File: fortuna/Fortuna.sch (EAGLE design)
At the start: 36 parts, among them M1 MOTOR20MM, M2 MOTOR20MM, Q1 600mA/40V, Q2 600mA/40V, U2 OPA2343UA, U3 OPA2343UA

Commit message: Finish fortuna schematic
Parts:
- removed C1, C2: 10uF, SparkFun-Capacitors:10UF-POLAR-RADIAL-2.5MM-25V-20%
- removed U1: (no value), SparkFun-IC-Power:V_REG_78XX-TO-220
- C3: value 1uF -> 1μF
- D3: value (none) -> LLED
- D4: value (none) -> RLED
- R1, R10, R2, R3, R4, R5, R6: value 2.7k -> 2.7kΩ
- R11: value 100k -> 100kΩ
- R12, R13, R9: value 10k -> 10kΩ
- R14, R15: value 1k -> 1kΩ
- R16, R17: value 300 -> 300Ω
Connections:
- net N$11 renamed -RPHOTO
- net N$12 renamed D2
- net N$14 renamed -MIC
- net N$15 renamed A3
- net N$25 renamed D5
- net N$26 renamed D10
- net N$4 renamed +MIC
- net N$6 renamed +RPHOTO
- net N$7 renamed -LPHOTO
- net N$9 renamed +LPHOTO
- removed net N$1 (its old number): B1.VIN, C1.+, D1.C, D2.C, G1.+, M1.+, M2.+, R9.2, U1.IN
- removed net N$10 (its old number): B1.A0, R1.1, R7.P$2
- removed net N$16: B1.D4, D3.A, U2.OUT_A
- removed net N$19: B1.D7, D4.A, U3.OUT_A
- removed net N$2 (its old number): B1.GND@0, C1.-, C2.-, G1.-, LS1.1, MK1.2, Q1.E, Q2.E, R12.1, R16.1, R17.1, R2.1, R3.2, R5.1, R6.1, U1.GND, U2.V-, U3.V-
- removed net N$22: B1.A5, R4.2, R8.P$2
- removed net N$3: C2.+, R13.1, U1.OUT, U2.V+, U3.V+
- removed net N$5: LS1.2, U3.-IN_B, U3.OUT_B
- new net 5V: B1.5V, R1.1, R13.1, R4.2, R7.P$2, R8.P$2, U2.V+, U3.V+
- new net A0: B1.A0, D3.A, U2.OUT_A
- new net A5: B1.A5, D4.A, U3.OUT_A
- new net GND: B1.GND@2, G1.-, LS1.2, MK1.2, Q1.E, Q2.E, R12.1, R16.1, R17.1, R2.1, R3.2, R5.1, R6.1, U2.V-, U3.V-
- new net OUT_BUZZER: LS1.1, U3.-IN_B, U3.OUT_B
- new net VIN: B1.VIN, D1.C, D2.C, G1.+, M1.+, M2.+, R9.2
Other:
- note added: "+BUZZER"
- note added: "-BUZZER"
- note added: "OUT_LPHOTO"
- note added: "OUT_MIC"
- note added: "OUT_RPHOTO"
- moved on the sheet: B1, C3, D1, D2, D3, D4, G1, LS1, M1, M2, MK1, Q1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

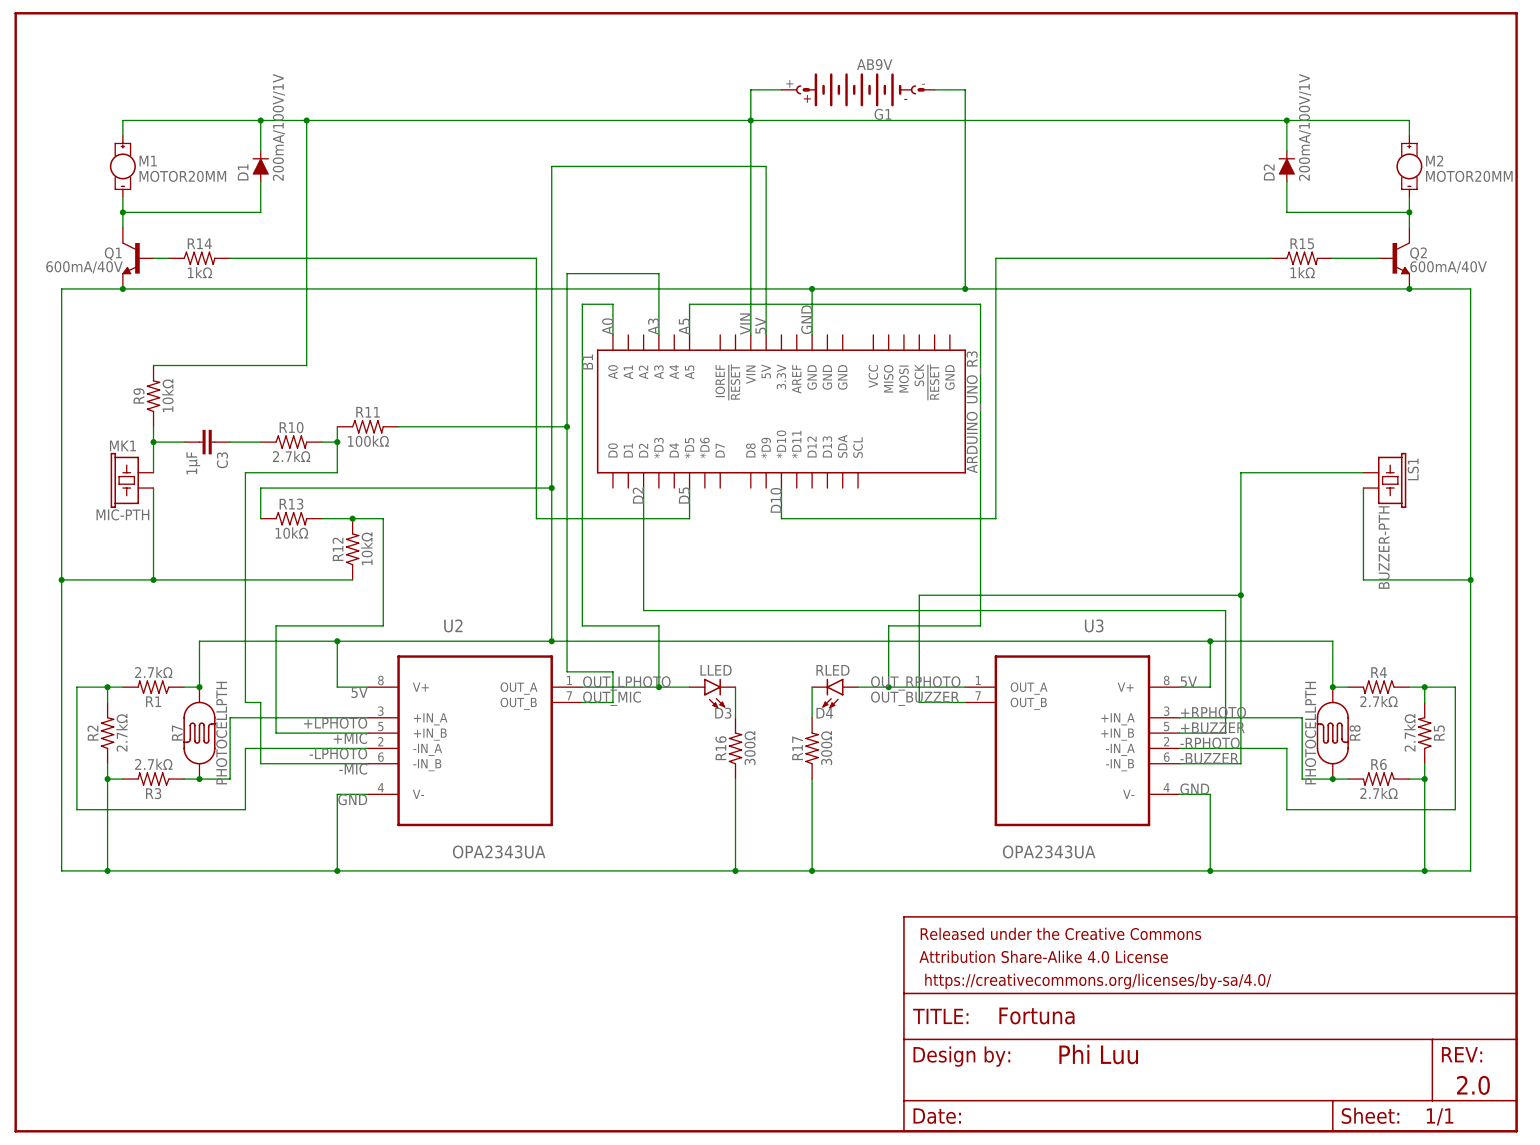
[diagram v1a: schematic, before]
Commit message: Change battery Fortuna
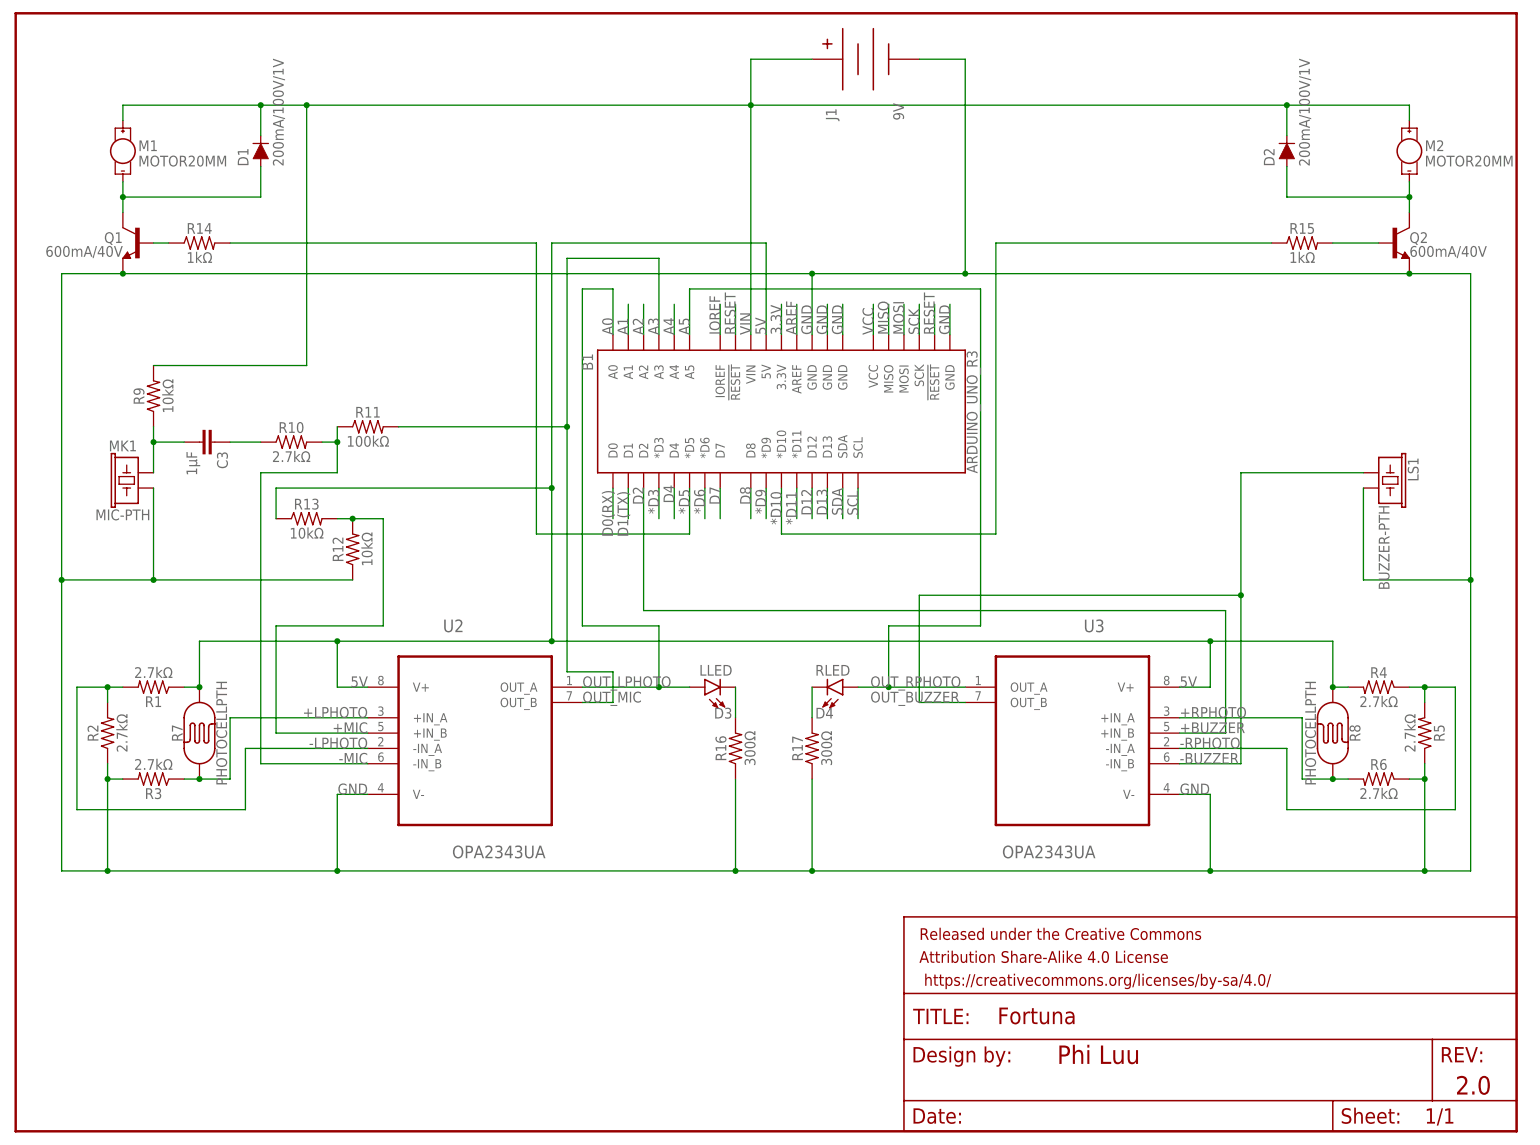
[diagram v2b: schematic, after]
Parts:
- removed G1: AB9V, battery:AB9V
- added J1: 9V, SparkFun-Connectors:BC9VPC
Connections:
- net D10 renamed *D10
- net D5 renamed *D5
- new net *D11: B1.*D11
- new net *D3: B1.*D3
- new net *D6: B1.*D6
- new net *D9: B1.*D9
- new net 3.3V: B1.3.3V
- new net A1: B1.A1
- new net A2: B1.A2
- new net A4: B1.A4
- new net AREF: B1.AREF
- new net D0(RX): B1.D0
- new net D1(TX): B1.D1
- new net D12: B1.D12
- new net D13: B1.D13
- new net D4: B1.D4
- new net D7: B1.D7
- new net D8: B1.D8
- new net IOREF: B1.IOREF
- new net MISO: B1.MISO
- new net MOSI: B1.MOSI
- new net RESET: B1.!RESET!@1, B1.!RESET!@2
- new net SCK: B1.SCK
- new net SCL: B1.SCL
- new net SDA: B1.SDA
- new net VCC: B1.VCC
- net GND: now also B1.GND, B1.GND@0, B1.GND@1, J1.V-; no longer G1.-
- net VIN: now also J1.V+; no longer G1.+
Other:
- moved on the sheet: D1, D2, M1, M2, Q1, Q2, R13, R14, R15

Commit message: Follow naming convention - English letter only
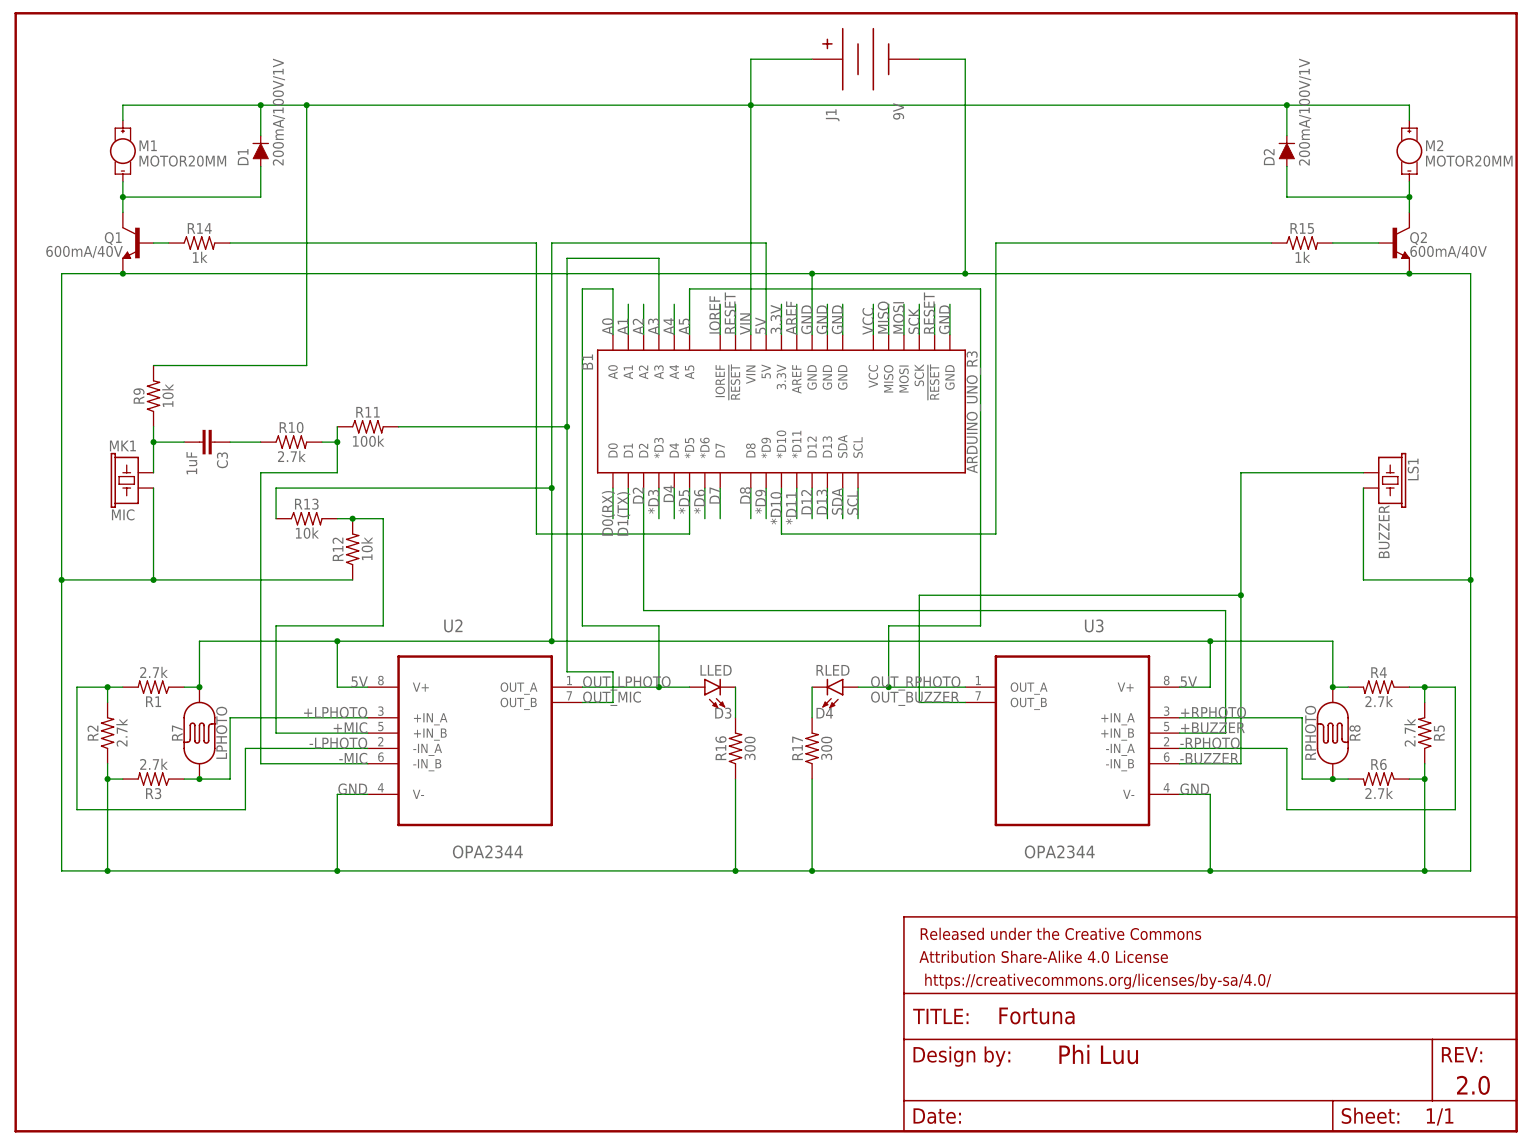
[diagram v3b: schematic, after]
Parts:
- C3: value 1μF -> 1uF
- LS1: value BUZZER-PTH -> BUZZER
- MK1: value MIC-PTH -> MIC
- R1, R10, R2, R3, R4, R5, R6: value 2.7kΩ -> 2.7k
- R11: value 100kΩ -> 100k
- R12, R13, R9: value 10kΩ -> 10k
- R14, R15: value 1kΩ -> 1k
- R16, R17: value 300Ω -> 300
- R7: value PHOTOCELLPTH -> LPHOTO
- R8: value PHOTOCELLPTH -> RPHOTO
- U2, U3: value OPA2343UA -> OPA2344
